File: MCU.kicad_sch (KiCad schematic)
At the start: 14 parts, among them U4 EFM32GG332, Y1 Crystal_GND23

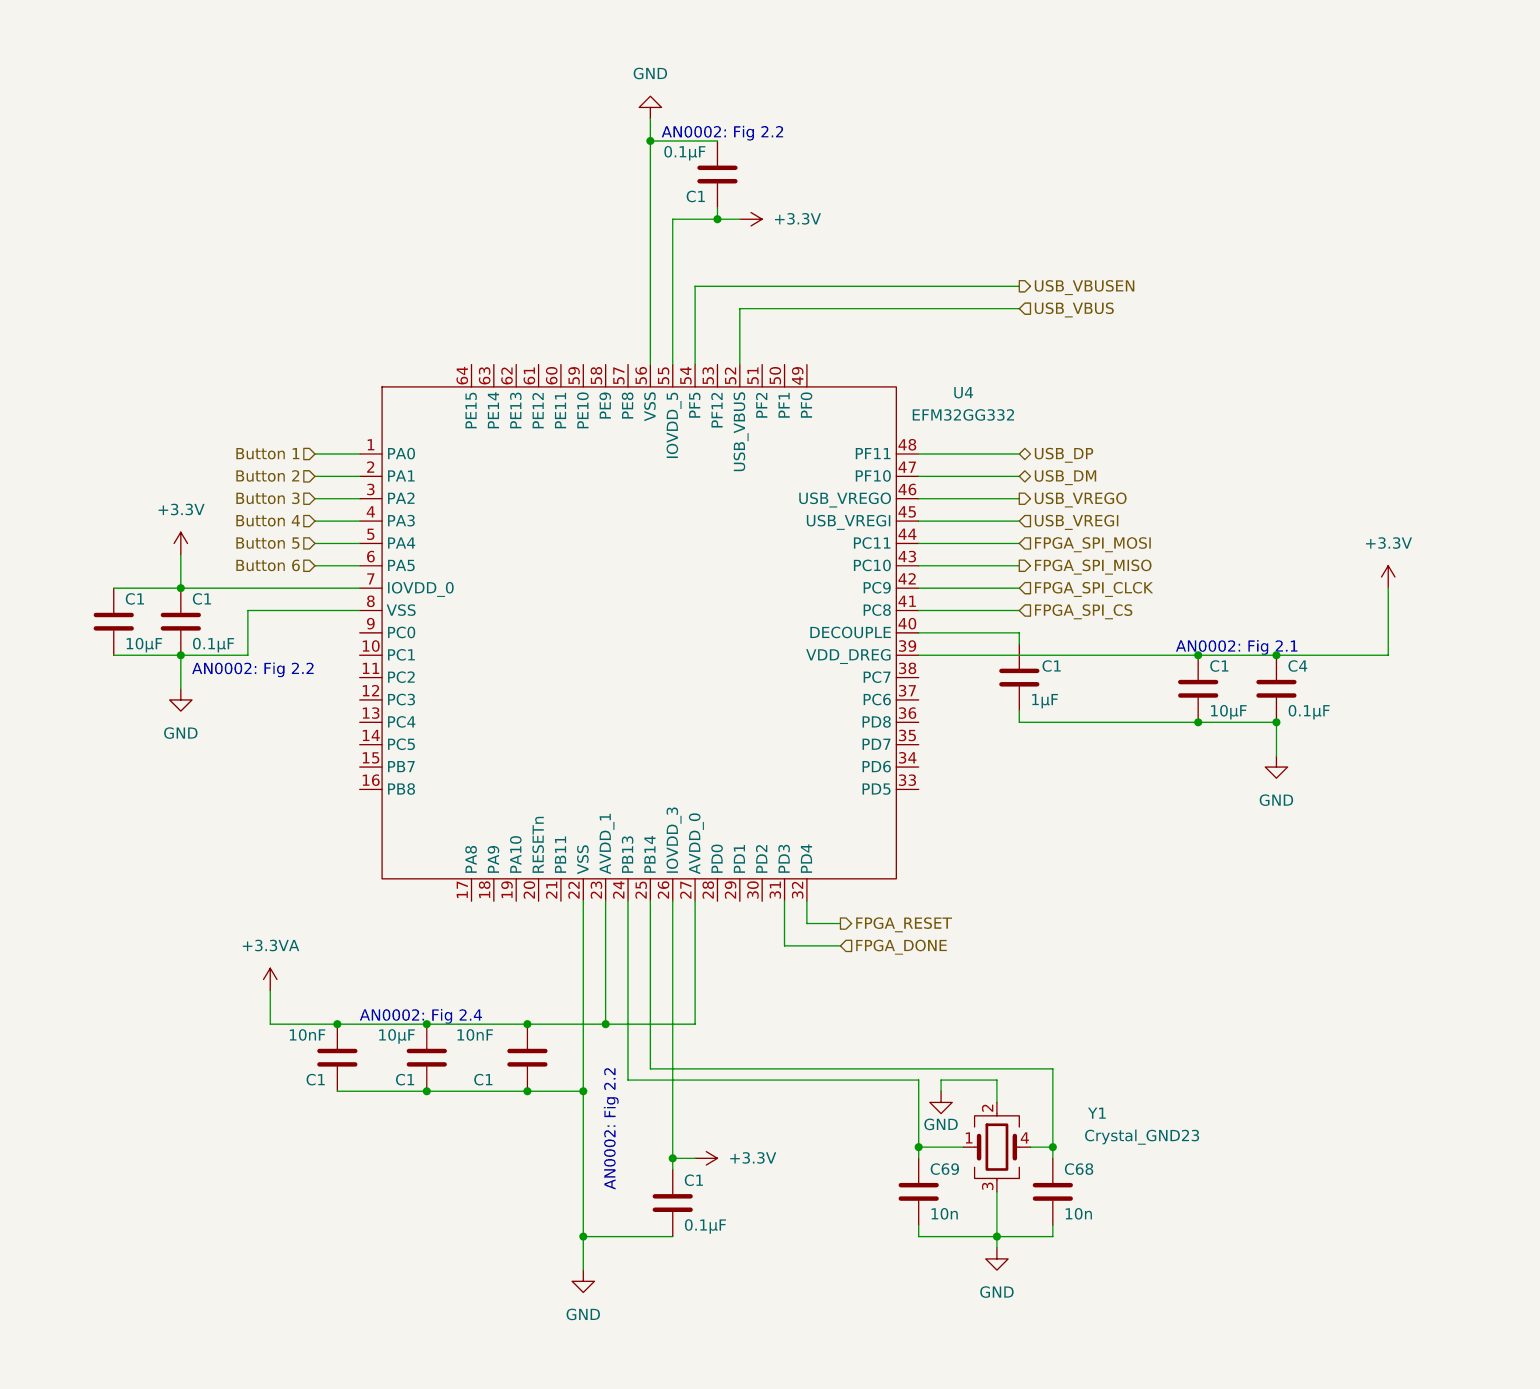
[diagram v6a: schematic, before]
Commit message: add MCU JTAG Debugger
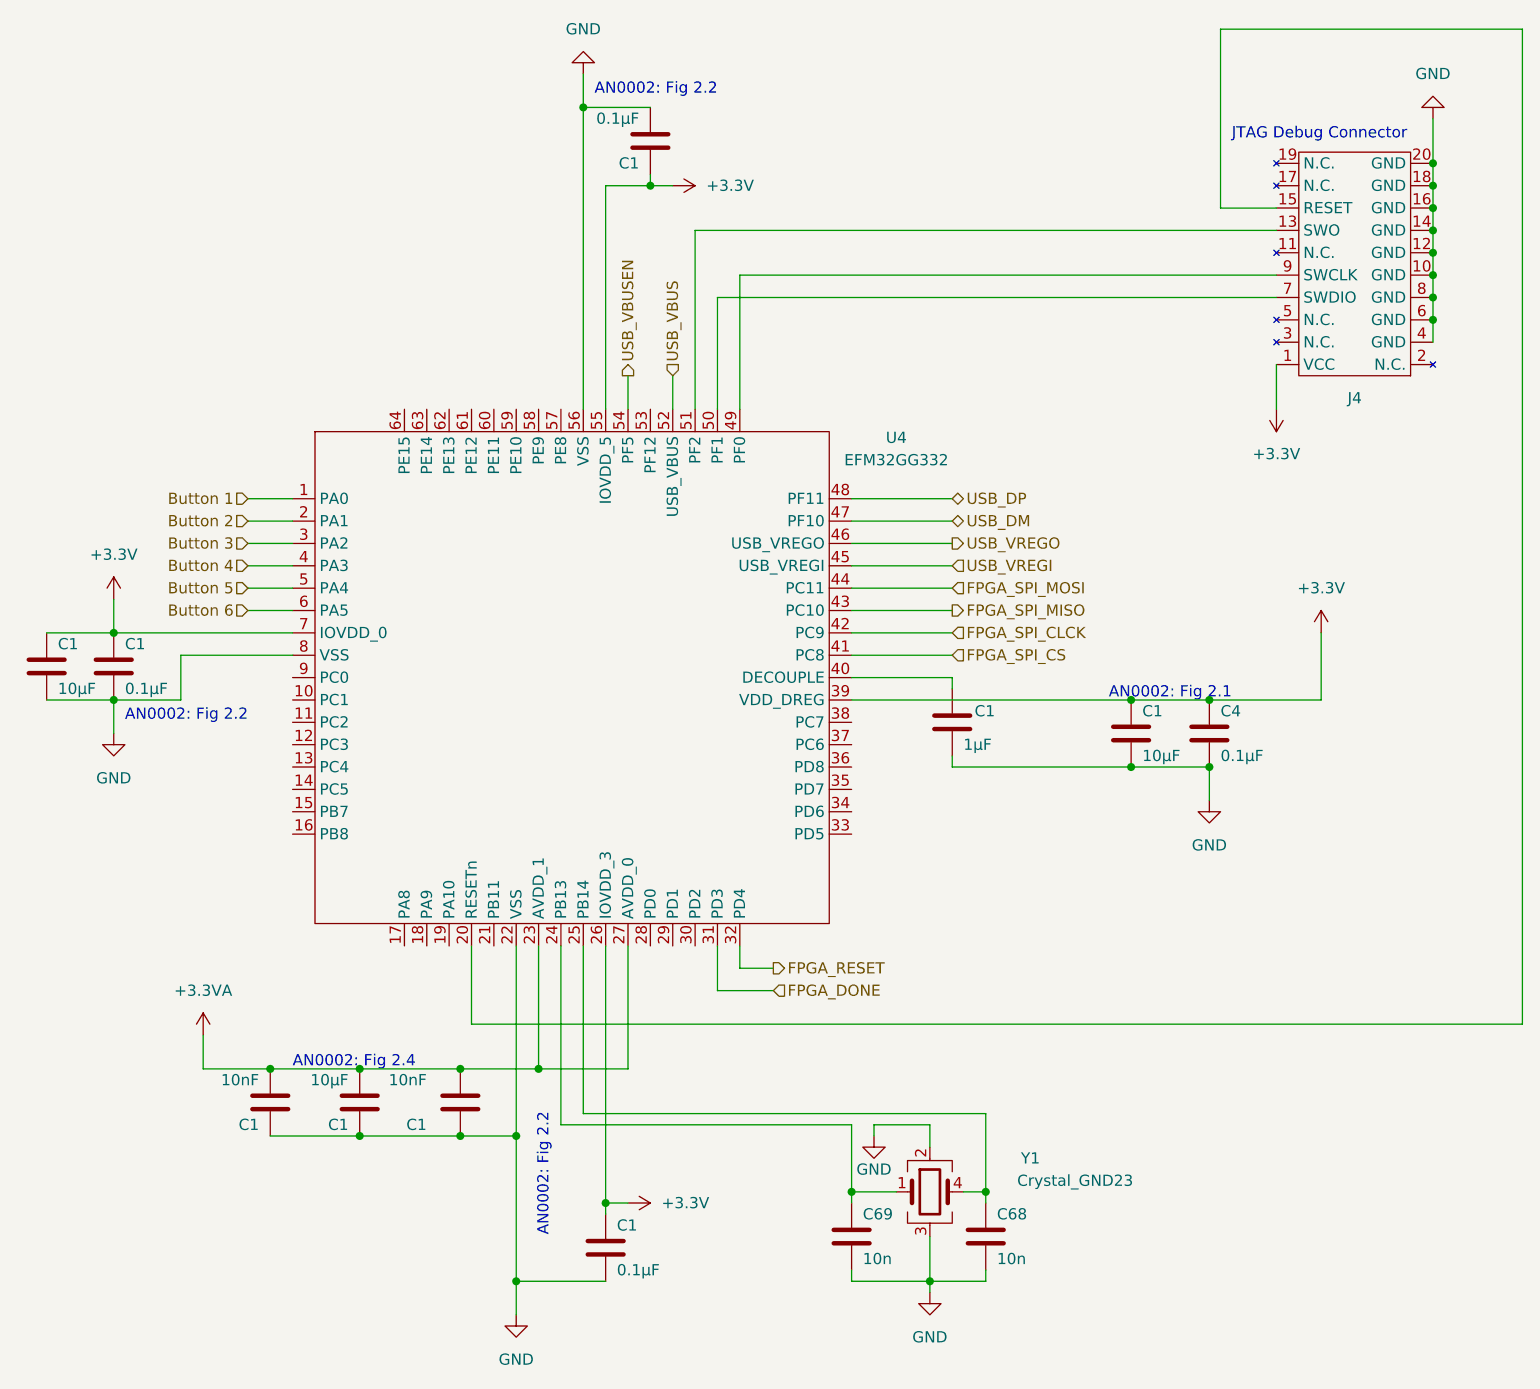
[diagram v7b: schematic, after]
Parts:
- added J4: ~, symbol GuitarZero:MCU_JTAG_Connector
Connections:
- net +3.3V: now also J4.1 (VCC)
- net GND: now also J4.10 (GND), J4.12 (GND), J4.14 (GND), J4.16 (GND), J4.18 (GND), J4.20 (GND), J4.4 (GND), J4.6 (GND), J4.8 (GND)
- net at U4.20 (RESETn): now also J4.15 (RESET)
- net at U4.49 (PF0): now also J4.9 (SWCLK)
- net at U4.50 (PF1): now also J4.7 (SWDIO)
- net at U4.51 (PF2): now also J4.13 (SWO)
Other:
- note added: "JTAG Debug Connector"
- moved on the sheet: C1, C4, C68, C69, U4, Y1
